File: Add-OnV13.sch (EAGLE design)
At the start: 10 parts, among them X1 1501_03

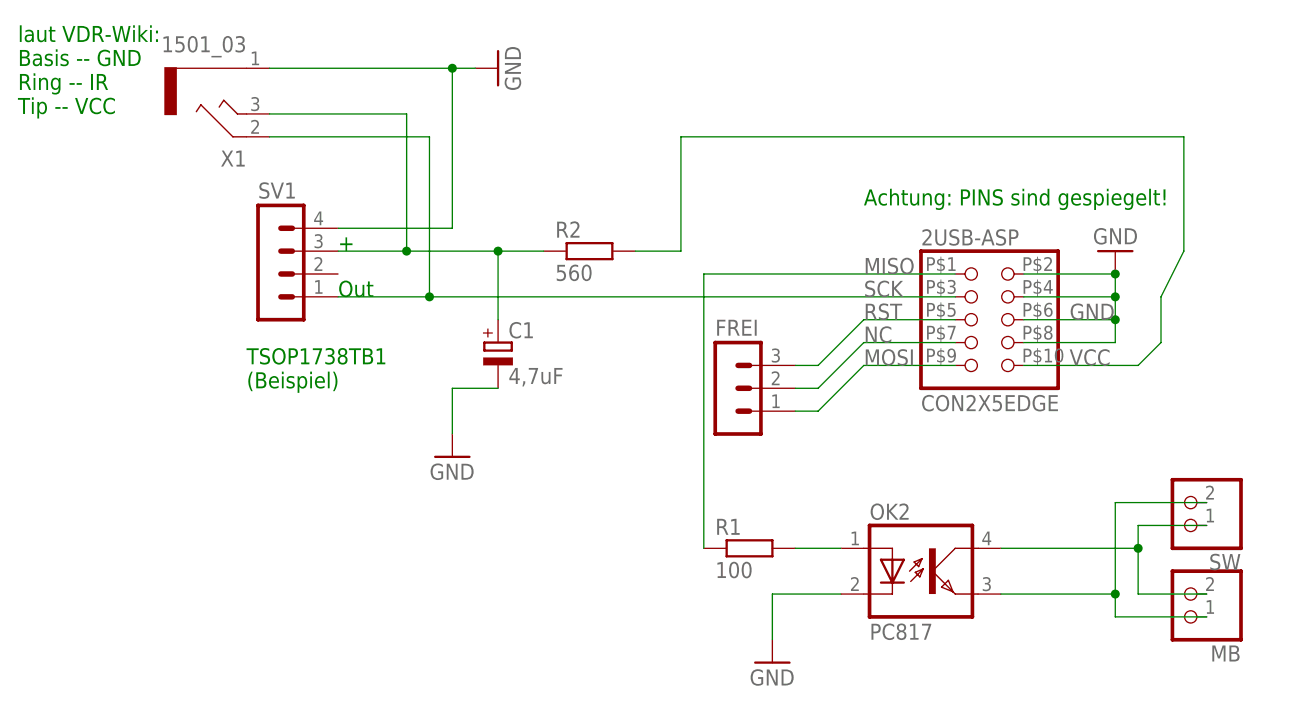
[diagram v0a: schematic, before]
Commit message: Mirrored Plug
for using the the cable of USB-ASP...
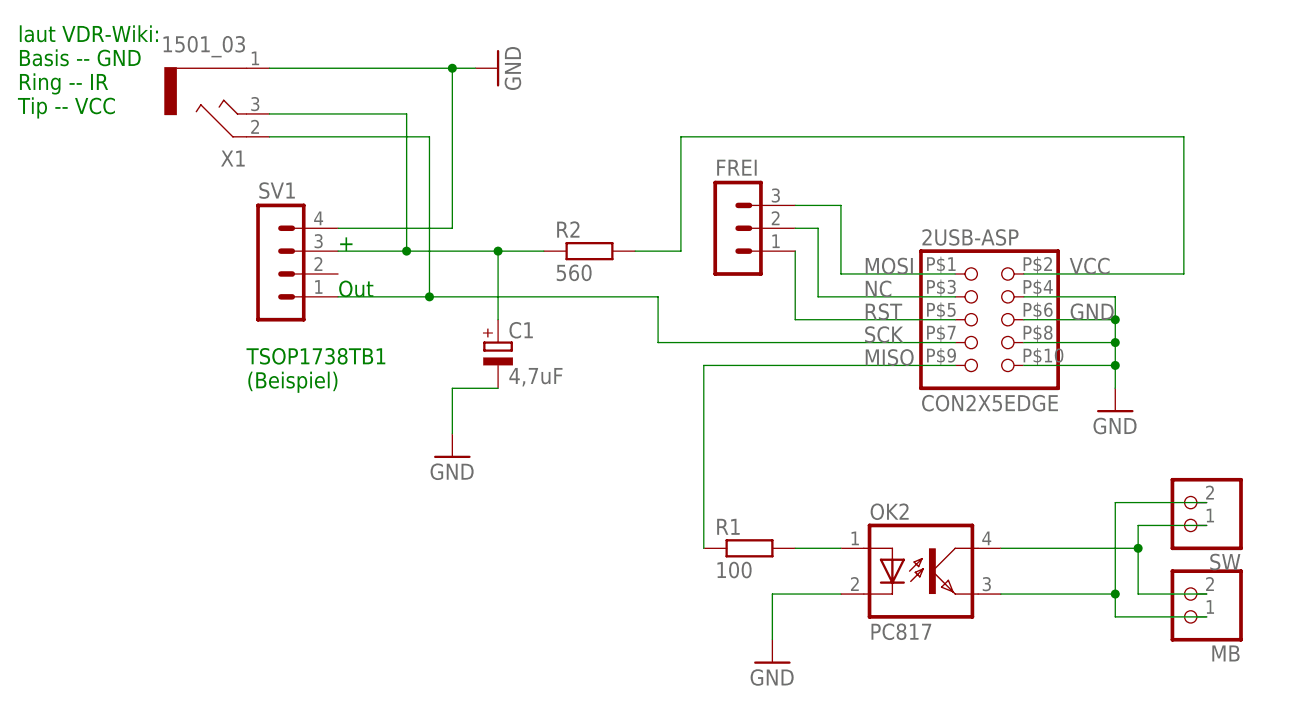
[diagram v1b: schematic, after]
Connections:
- net GND: now also 2USB-ASP.10; no longer 2USB-ASP.2
- net MISO: now also 2USB-ASP.9; no longer 2USB-ASP.1
- net MOSI: now also 2USB-ASP.1, FREI.3; no longer 2USB-ASP.9, FREI.1
- net NC: now also 2USB-ASP.3; no longer 2USB-ASP.7
- net RST: now also FREI.1; no longer FREI.3
- net SCK: now also 2USB-ASP.7; no longer 2USB-ASP.3
- net VCC: now also 2USB-ASP.2; no longer 2USB-ASP.10
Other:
- note removed: "Achtung: PINS sind gespiegelt!"
- moved on the sheet: FREI
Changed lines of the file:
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@@
 <sheet>
 <plain>
-<text x="-5.08" y="124.46" size="1.778" layer="91">Achtung: PINS sind gespiegelt!</text>
 <text x="-63.5" y="114.3" size="1.778" layer="91">Out</text>
 <text x="-63.5" y="119.38" size="1.778" layer="91">+</text>
@@
 <instance part="C1" gate="G$1" x="-45.72" y="109.22"/>
 <instance part="GND1" gate="1" x="-50.8" y="96.52"/>
-<instance part="GND2" gate="1" x="22.86" y="119.38" rot="R180"/>
-<instance part="FREI" gate="G$1" x="-20.32" y="104.14"/>
+<instance part="GND2" gate="1" x="22.86" y="101.6"/>
+<instance part="FREI" gate="G$1" x="-20.32" y="121.92"/>
 <instance part="GND3" gate="1" x="-15.24" y="73.66"/>
 <instance part="SW" gate="G$1" x="30.48" y="91.44" rot="R180"/>
@@
 <net name="SCK" class="0">
 <segment>
-<label x="-5.08" y="114.3" size="1.778" layer="95"/>
-<pinref part="2USB-ASP" gate="G$1" pin="3"/>
 <wire x1="-63.5" y1="114.3" x2="-53.34" y2="114.3" width="0.1524" layer="91"/>
 <pinref part="SV1" gate="1" pin="1"/>
 <pinref part="X1" gate="G$1" pin="2"/>
-<wire x1="-53.34" y1="114.3" x2="5.08" y2="114.3" width="0.1524" layer="91"/>
 <wire x1="-71.12" y1="132.08" x2="-53.34" y2="132.08" width="0.1524" layer="91"/>
 <wire x1="-53.34" y1="132.08" x2="-53.34" y2="114.3" width="0.1524" layer="91"/>
+<wire x1="-53.34" y1="114.3" x2="-27.94" y2="114.3" width="0.1524" layer="91"/>
+<wire x1="-27.94" y1="114.3" x2="-27.94" y2="109.22" width="0.1524" layer="91"/>
 <junction x="-53.34" y="114.3"/>
-</segment>
-</net>
-<net name="MISO" class="0">
-<segment>
-<pinref part="R1" gate="G$1" pin="1"/>
-<wire x1="-22.86" y1="86.36" x2="-22.86" y2="116.84" width="0.1524" layer="91"/>
-<pinref part="2USB-ASP" gate="G$1" pin="1"/>
-<wire x1="-22.86" y1="116.84" x2="5.08" y2="116.84" width="0.1524" layer="91"/>
-<label x="-5.08" y="116.84" size="1.778" layer="95"/>
+<pinref part="2USB-ASP" gate="G$1" pin="7"/>
+<label x="-5.08" y="109.22" size="1.778" layer="95"/>
+<wire x1="-27.94" y1="109.22" x2="5.08" y2="109.22" width="0.1524" layer="91"/>
 </segment>
 </net>
@@
 </segment>
 <segment>
+<pinref part="GND4" gate="1" pin="GND"/>
+<pinref part="X1" gate="G$1" pin="1"/>
+<wire x1="-48.26" y1="139.7" x2="-50.8" y2="139.7" width="0.1524" layer="91"/>
+<wire x1="-50.8" y1="139.7" x2="-71.12" y2="139.7" width="0.1524" layer="91"/>
+<wire x1="-50.8" y1="139.7" x2="-50.8" y2="121.92" width="0.1524" layer="91"/>
+<junction x="-50.8" y="139.7"/>
+<pinref part="SV1" gate="1" pin="4"/>
+<wire x1="-50.8" y1="121.92" x2="-63.5" y2="121.92" width="0.1524" layer="91"/>
+</segment>
+<segment>
 <pinref part="2USB-ASP" gate="G$1" pin="8"/>
 <wire x1="12.7" y1="109.22" x2="22.86" y2="109.22" width="0.1524" layer="91"/>
@@
 <wire x1="22.86" y1="109.22" x2="22.86" y2="111.76" width="0.1524" layer="91"/>
 <junction x="22.86" y="111.76"/>
+<label x="17.78" y="111.76" size="1.778" layer="95"/>
 <pinref part="GND2" gate="1" pin="GND"/>
-<wire x1="22.86" y1="116.84" x2="22.86" y2="114.3" width="0.1524" layer="91"/>
-<junction x="22.86" y="114.3"/>
-<pinref part="2USB-ASP" gate="G$1" pin="2"/>
-<wire x1="12.7" y1="116.84" x2="22.86" y2="116.84" width="0.1524" layer="91"/>
-<junction x="22.86" y="116.84"/>
-<label x="17.78" y="111.76" size="1.778" layer="95"/>
-</segment>
-<segment>
-<pinref part="GND4" gate="1" pin="GND"/>
-<pinref part="X1" gate="G$1" pin="1"/>
-<wire x1="-48.26" y1="139.7" x2="-50.8" y2="139.7" width="0.1524" layer="91"/>
-<wire x1="-50.8" y1="139.7" x2="-71.12" y2="139.7" width="0.1524" layer="91"/>
-<wire x1="-50.8" y1="139.7" x2="-50.8" y2="121.92" width="0.1524" layer="91"/>
-<junction x="-50.8" y="139.7"/>
-<pinref part="SV1" gate="1" pin="4"/>
-<wire x1="-50.8" y1="121.92" x2="-63.5" y2="121.92" width="0.1524" layer="91"/>
+<wire x1="22.86" y1="104.14" x2="22.86" y2="106.68" width="0.1524" layer="91"/>
+<junction x="22.86" y="109.22"/>
+<pinref part="2USB-ASP" gate="G$1" pin="10"/>
+<wire x1="22.86" y1="106.68" x2="22.86" y2="109.22" width="0.1524" layer="91"/>
+<wire x1="12.7" y1="106.68" x2="22.86" y2="106.68" width="0.1524" layer="91"/>
+<junction x="22.86" y="106.68"/>
 </segment>
 </net>
@@
 <pinref part="R2" gate="G$1" pin="2"/>
 <wire x1="-25.4" y1="119.38" x2="-30.48" y2="119.38" width="0.1524" layer="91"/>
-<wire x1="30.48" y1="132.08" x2="30.48" y2="119.38" width="0.1524" layer="91"/>
-<wire x1="30.48" y1="119.38" x2="27.94" y2="114.3" width="0.1524" layer="91"/>
-<wire x1="27.94" y1="114.3" x2="27.94" y2="109.22" width="0.1524" layer="91"/>
-<wire x1="27.94" y1="109.22" x2="25.4" y2="106.68" width="0.1524" layer="91"/>
-<pinref part="2USB-ASP" gate="G$1" pin="10"/>
-<wire x1="25.4" y1="106.68" x2="12.7" y2="106.68" width="0.1524" layer="91"/>
-<label x="17.78" y="106.68" size="1.778" layer="95"/>
+<wire x1="30.48" y1="132.08" x2="30.48" y2="116.84" width="0.1524" layer="91"/>
+<pinref part="2USB-ASP" gate="G$1" pin="2"/>
+<wire x1="30.48" y1="116.84" x2="12.7" y2="116.84" width="0.1524" layer="91"/>
+<label x="17.78" y="116.84" size="1.778" layer="95"/>
 </segment>
 </net>
@@
 <net name="RST" class="0">
 <segment>
+<pinref part="2USB-ASP" gate="G$1" pin="5"/>
+<wire x1="-12.7" y1="111.76" x2="5.08" y2="111.76" width="0.1524" layer="91"/>
+<label x="-5.08" y="111.76" size="1.778" layer="95"/>
+<pinref part="FREI" gate="G$1" pin="1"/>
+<wire x1="-12.7" y1="119.38" x2="-12.7" y2="111.76" width="0.1524" layer="91"/>
+</segment>
+</net>
+<net name="MISO" class="0">
+<segment>
+<pinref part="2USB-ASP" gate="G$1" pin="9"/>
+<label x="-5.08" y="106.68" size="1.778" layer="95"/>
+<pinref part="R1" gate="G$1" pin="1"/>
+<wire x1="-22.86" y1="86.36" x2="-22.86" y2="106.68" width="0.1524" layer="91"/>
+<wire x1="-22.86" y1="106.68" x2="5.08" y2="106.68" width="0.1524" layer="91"/>
+</segment>
+</net>
+<net name="MOSI" class="0">
+<segment>
 <pinref part="FREI" gate="G$1" pin="3"/>
-<wire x1="-12.7" y1="106.68" x2="-10.16" y2="106.68" width="0.1524" layer="91"/>
-<wire x1="-10.16" y1="106.68" x2="-5.08" y2="111.76" width="0.1524" layer="91"/>
-<pinref part="2USB-ASP" gate="G$1" pin="5"/>
-<wire x1="-5.08" y1="111.76" x2="5.08" y2="111.76" width="0.1524" layer="91"/>
-<label x="-5.08" y="111.76" size="1.778" layer="95"/>
+<wire x1="-12.7" y1="124.46" x2="-7.62" y2="124.46" width="0.1524" layer="91"/>
+<wire x1="-7.62" y1="124.46" x2="-7.62" y2="116.84" width="0.1524" layer="91"/>
+<pinref part="2USB-ASP" gate="G$1" pin="1"/>
+<wire x1="-7.62" y1="116.84" x2="5.08" y2="116.84" width="0.1524" layer="91"/>
+<label x="-5.08" y="116.84" size="1.778" layer="95"/>
 </segment>
 </net>
@@
 <segment>
 <pinref part="FREI" gate="G$1" pin="2"/>
-<wire x1="-12.7" y1="104.14" x2="-10.16" y2="104.14" width="0.1524" layer="91"/>
-<wire x1="-10.16" y1="104.14" x2="-5.08" y2="109.22" width="0.1524" layer="91"/>
-<pinref part="2USB-ASP" gate="G$1" pin="7"/>
-<wire x1="-5.08" y1="109.22" x2="5.08" y2="109.22" width="0.1524" layer="91"/>
-<label x="-5.08" y="109.22" size="1.778" layer="95"/>
+<wire x1="-12.7" y1="121.92" x2="-10.16" y2="121.92" width="0.1524" layer="91"/>
+<wire x1="-10.16" y1="121.92" x2="-10.16" y2="114.3" width="0.1524" layer="91"/>
+<pinref part="2USB-ASP" gate="G$1" pin="3"/>
+<wire x1="-10.16" y1="114.3" x2="5.08" y2="114.3" width="0.1524" layer="91"/>
+<label x="-5.08" y="114.3" size="1.778" layer="95"/>
 </segment>
 </net>
-<net name="MOSI" class="0">
-<segment>
-<pinref part="FREI" gate="G$1" pin="1"/>
-<wire x1="-12.7" y1="101.6" x2="-10.16" y2="101.6" width="0.1524" layer="91"/>
-<wire x1="-10.16" y1="101.6" x2="-5.08" y2="106.68" width="0.1524" layer="91"/>
-<pinref part="2USB-ASP" gate="G$1" pin="9"/>
-<wire x1="-5.08" y1="106.68" x2="5.08" y2="106.68" width="0.1524" layer="91"/>
-<label x="-5.08" y="106.68" size="1.778" layer="95"/>
-</segment>
-</net>
